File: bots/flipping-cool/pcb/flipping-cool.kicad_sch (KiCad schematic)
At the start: 0 parts

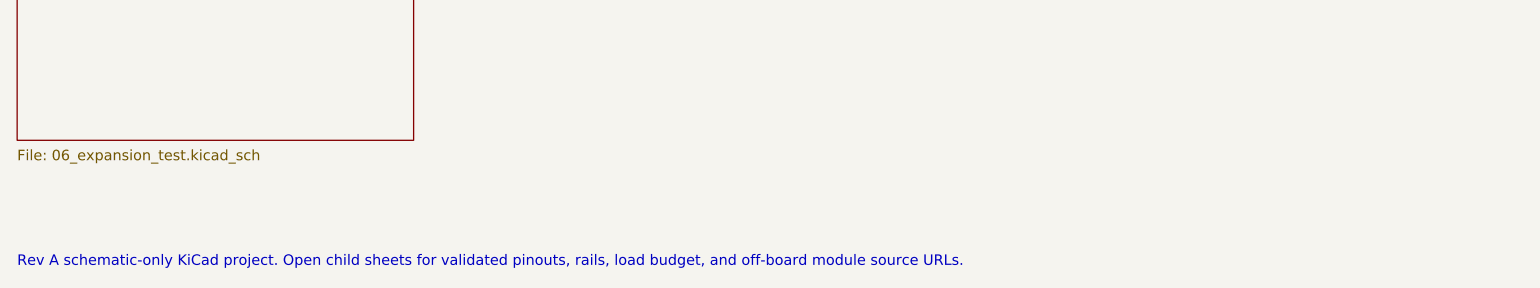
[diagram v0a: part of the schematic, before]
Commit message: Refactor Flipping Cool PCB design to Rev B, integrating active electrical features including ESP32-S3 module, power management, and control authority. Update documentation to reflect new architecture and validation requirements, while preserving Rev A historical context.
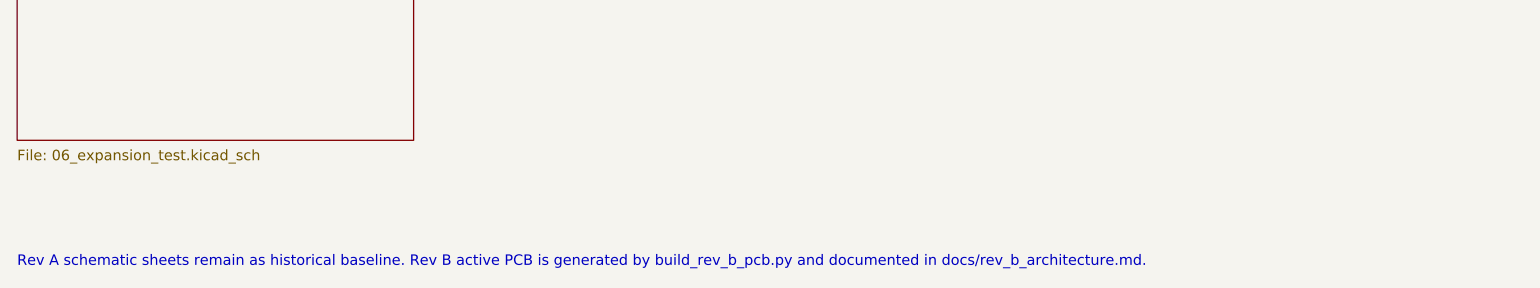
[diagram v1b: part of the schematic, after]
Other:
- note added: "Rev A schematic sheets remain as historical baseline. Rev B active PCB is generated by build_rev_b_pcb.py and documented in docs/rev_b_architecture.md."
- note removed: "Rev A schematic-only KiCad project. Open child sheets for validated pinouts, rails, load budget, and off-board module source URLs."
- title: Flipping Cool Rev A - Power Interconnect Root -> Flipping Cool Rev A Historical Sheets / Rev B PCB Generated
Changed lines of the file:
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@@
   (paper "A4")
   (title_block
-    (title "Flipping Cool Rev A - Power Interconnect Root")
+    (title "Flipping Cool Rev A Historical Sheets / Rev B PCB Generated")
     (date "2026-05-08")
     (rev "A")
@@
     (instances (project "flipping-cool" (path "/f81cc6b7-8d4a-56f1-ac66-4ebad2f24264" (page "8"))))
   )
-  (text "Rev A schematic-only KiCad project. Open child sheets for validated pinouts, rails, load budget, and off-board module source URLs."
+  (text "Rev A schematic sheets remain as historical baseline. Rev B active PCB is generated by build_rev_b_pcb.py and documented in docs/rev_b_architecture.md."
     (at 20.00 135.00 0)
     (effects (font (size 1.27 1.27)) (justify left top))

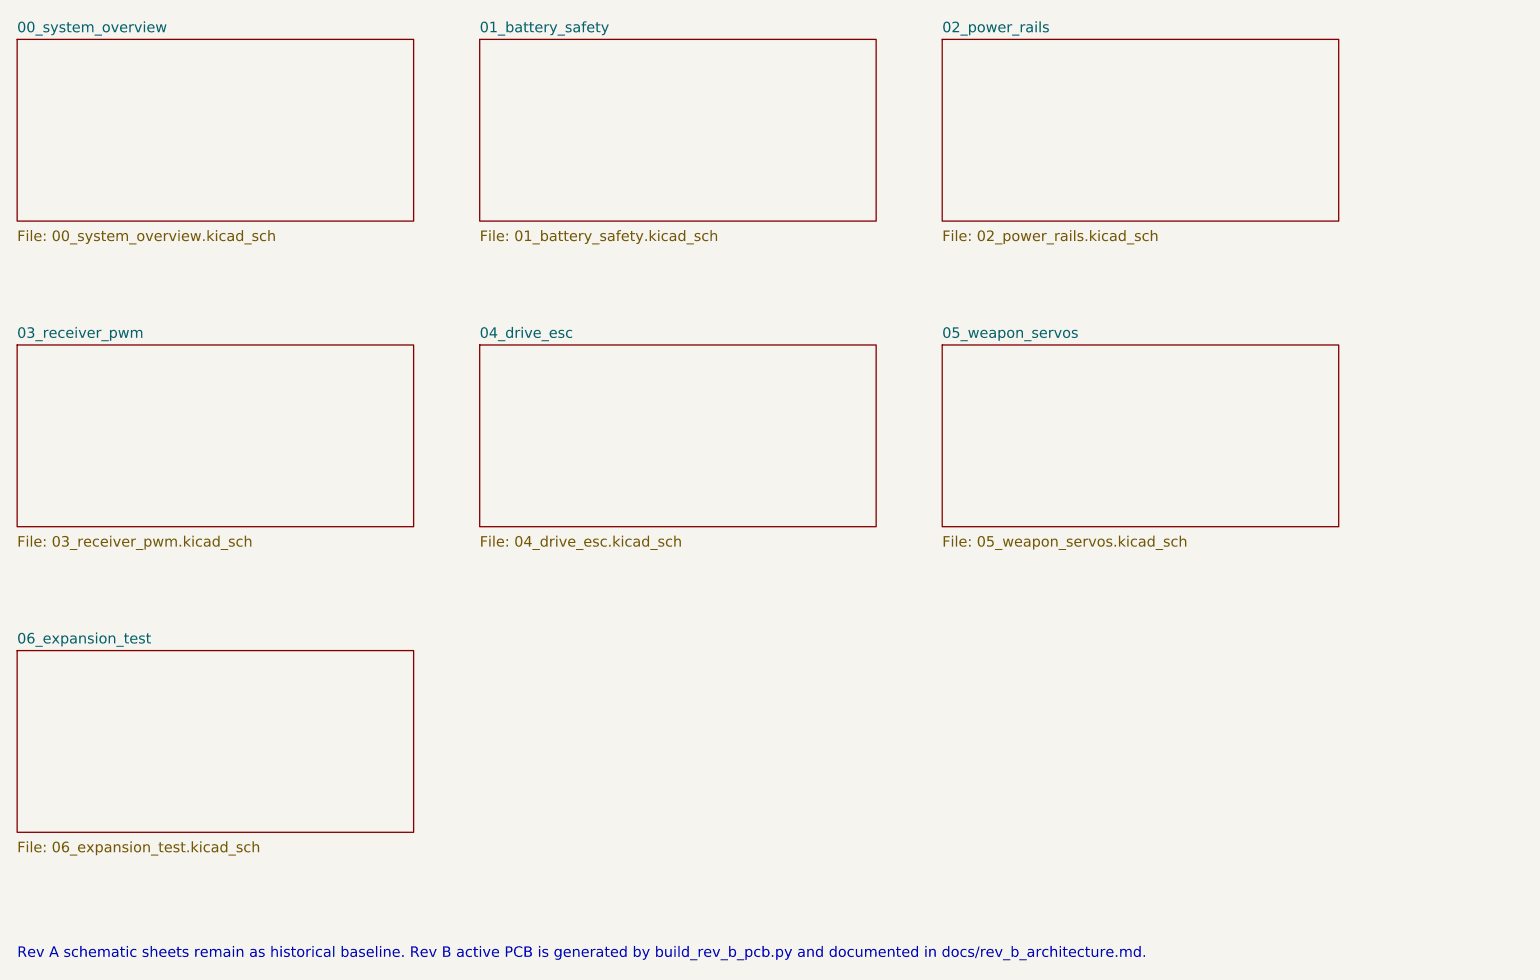
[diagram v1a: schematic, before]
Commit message: Refactor Flipping Cool PCB design to Rev B, updating title, date, and revision details. Integrate ESP32-S3 module and enhance documentation for MCU I/O and debugging features, while maintaining historical context from Rev A.
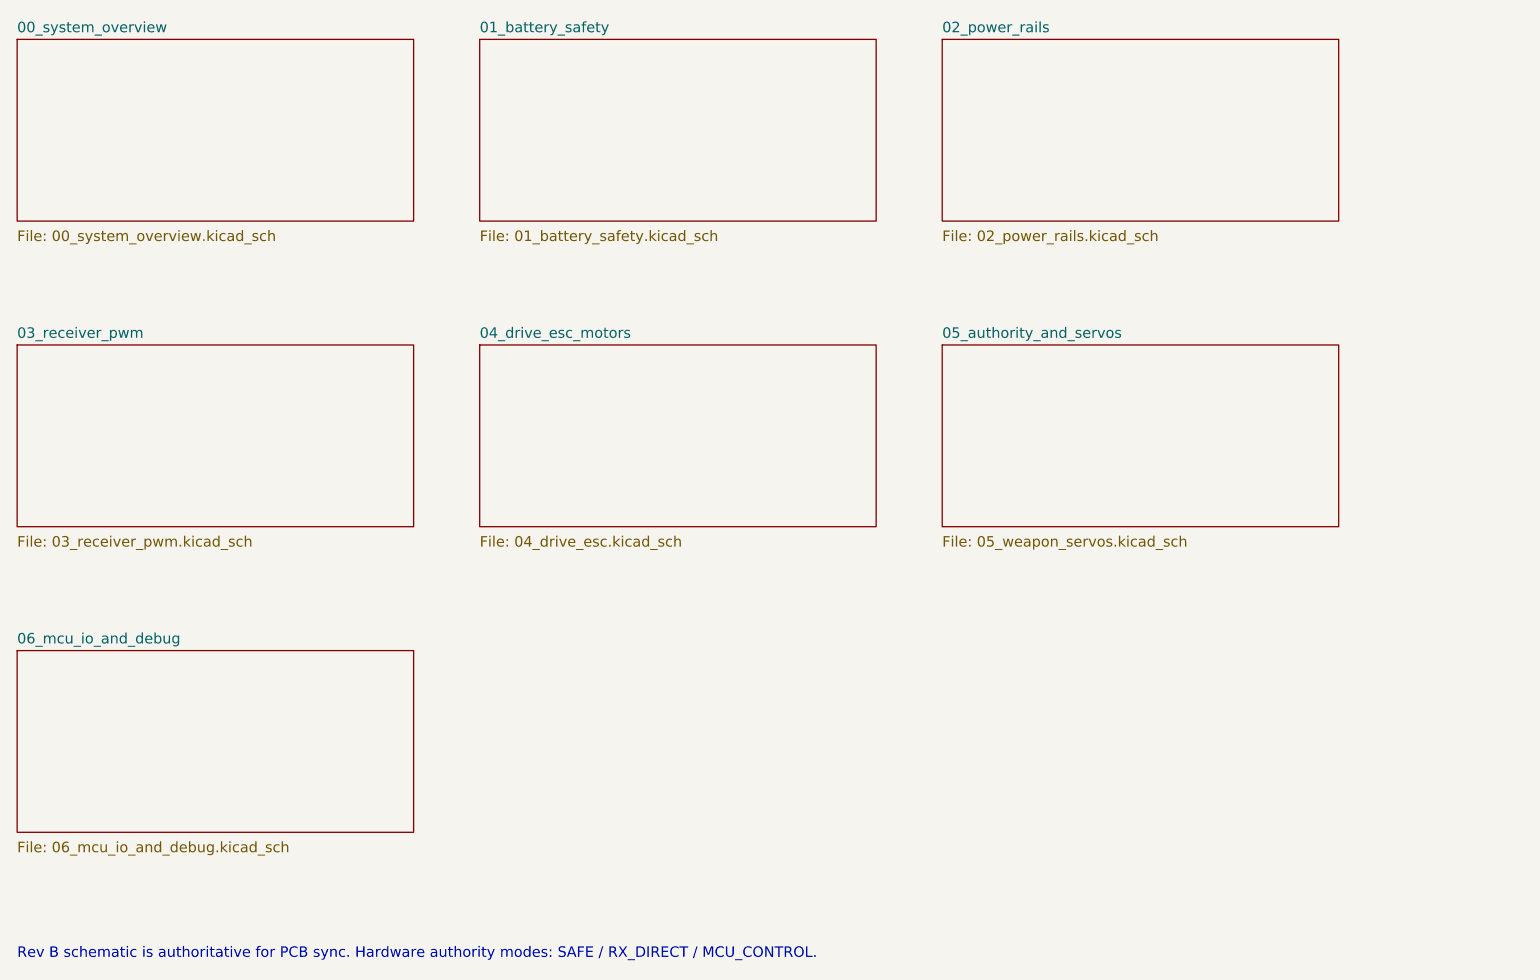
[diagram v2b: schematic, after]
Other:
- sheet 04_drive_esc renamed 04_drive_esc_motors
- sheet 05_weapon_servos renamed 05_authority_and_servos
- sheet 06_expansion_test renamed 06_mcu_io_and_debug
- sheet 06_mcu_io_and_debug: file 06_expansion_test.kicad_sch -> 06_mcu_io_and_debug.kicad_sch
- note added: "Rev B schematic is authoritative for PCB sync. Hardware authority modes: SAFE / RX_DIRECT / MCU_CONTROL."
- note removed: "Rev A schematic sheets remain as historical baseline. Rev B active PCB is generated by build_rev_b_pcb.py and documented in docs/rev_b_architecture.md."
- title: Flipping Cool Rev A Historical Sheets / Rev B PCB Generated -> Flipping Cool Rev B Integrated Control and Power
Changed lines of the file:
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@@
   (paper "A4")
   (title_block
-    (title "Flipping Cool Rev A Historical Sheets / Rev B PCB Generated")
-    (date "2026-05-08")
-    (rev "A")
+    (title "Flipping Cool Rev B Integrated Control and Power")
+    (date "2026-05-09")
+    (rev "B")
     (company "battle_bots_ai")
   )
@@
     (stroke (width 0.1524) (type solid))
     (fill (color 0 0 0 0.0000))
-    (property "Sheetname" "04_drive_esc"
+    (property "Sheetname" "04_drive_esc_motors"
       (at 76.00 61.29 0)
       (effects (font (size 1.27 1.27)) (justify left bottom))
@@
     (stroke (width 0.1524) (type solid))
     (fill (color 0 0 0 0.0000))
-    (property "Sheetname" "05_weapon_servos"
+    (property "Sheetname" "05_authority_and_servos"
       (at 132.00 61.29 0)
       (effects (font (size 1.27 1.27)) (justify left bottom))
@@
     (stroke (width 0.1524) (type solid))
     (fill (color 0 0 0 0.0000))
-    (property "Sheetname" "06_expansion_test"
+    (property "Sheetname" "06_mcu_io_and_debug"
       (at 20.00 98.29 0)
       (effects (font (size 1.27 1.27)) (justify left bottom))
     )
-    (property "Sheetfile" "06_expansion_test.kicad_sch"
+    (property "Sheetfile" "06_mcu_io_and_debug.kicad_sch"
       (at 20.00 122.08 0)
       (effects (font (size 1.27 1.27)) (justify left top))
@@
     (instances (project "flipping-cool" (path "/f81cc6b7-8d4a-56f1-ac66-4ebad2f24264" (page "8"))))
   )
-  (text "Rev A schematic sheets remain as historical baseline. Rev B active PCB is generated by build_rev_b_pcb.py and documented in docs/rev_b_architecture.md."
+  (text "Rev B schematic is authoritative for PCB sync. Hardware authority modes: SAFE / RX_DIRECT / MCU_CONTROL."
     (at 20.00 135.00 0)
     (effects (font (size 1.27 1.27)) (justify left top))
